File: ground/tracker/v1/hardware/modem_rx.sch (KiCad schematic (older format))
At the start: 15 parts, among them IC1 TCM3105, X1 4.4336 MHz

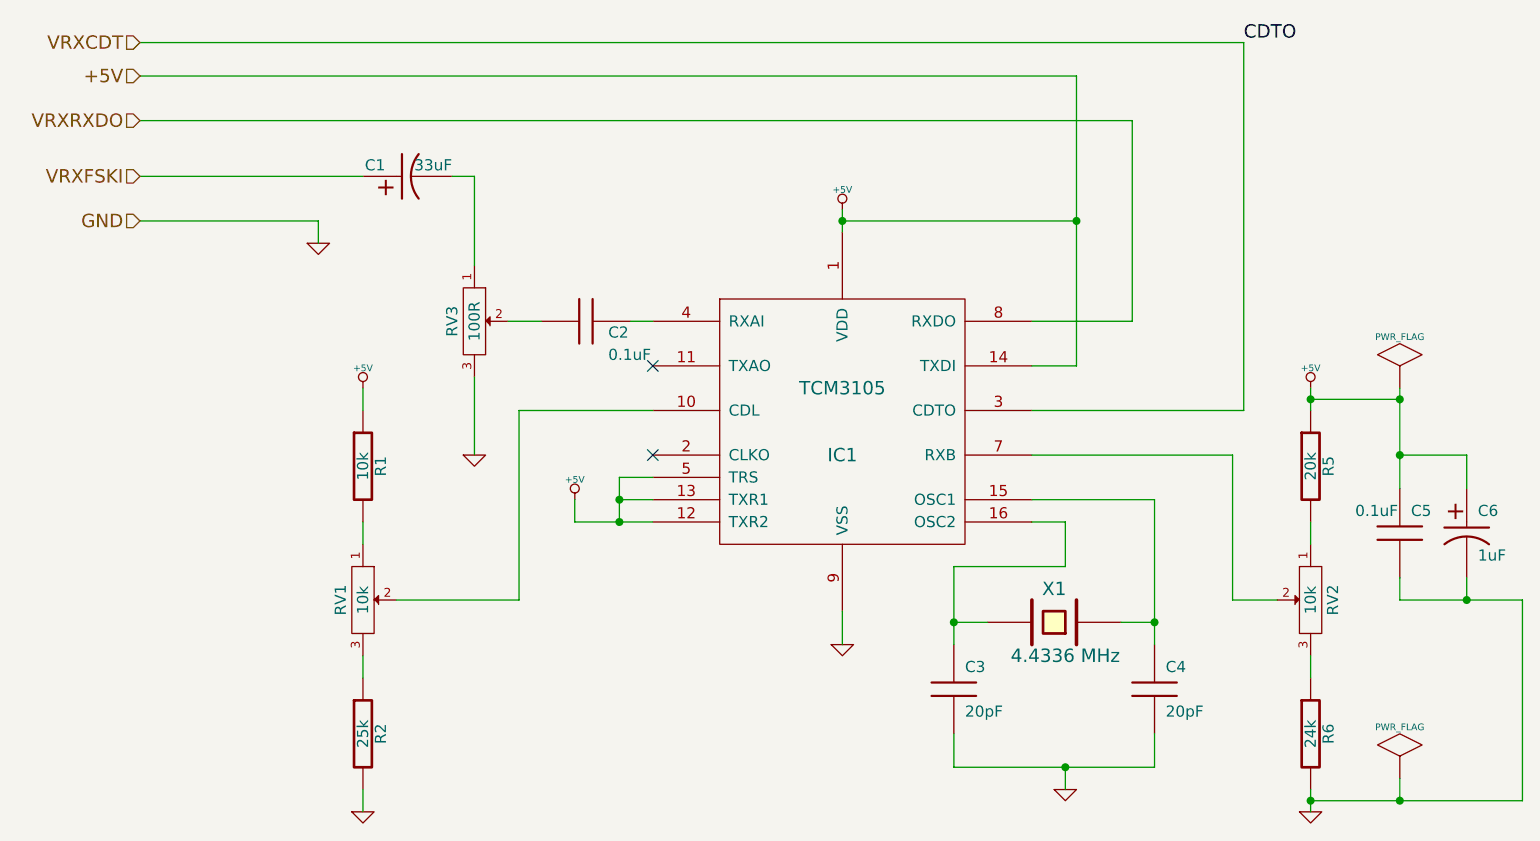
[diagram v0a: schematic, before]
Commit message: incorporated digital fsk demod routine, got flashhing lights, indicating getting data, now to test if tracking.EDIT: Tested in garden, and seems to track ok so fp context appears to be saving correctly^X
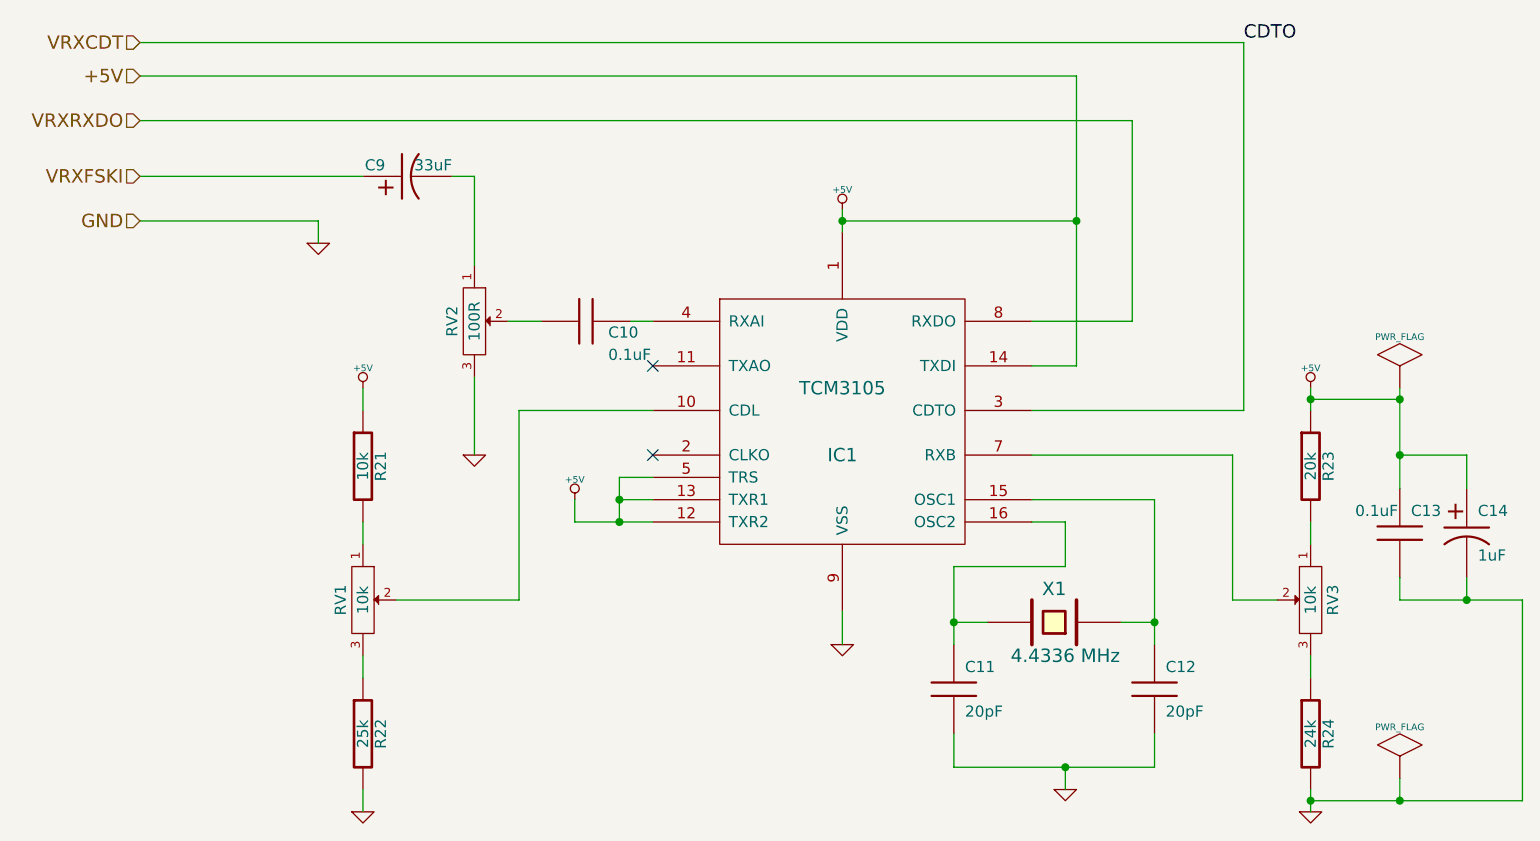
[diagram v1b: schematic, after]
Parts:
- renumbered C2 to C10, C3 to C11, C4 to C12, C5 to C13, C6 to C14, C1 to C9, R1 to R21, R2 to R22, R5 to R23, R6 to R24, RV3 to RV2, RV2 to RV3
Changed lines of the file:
@@
-EESchema Schematic File Version 2  date Thu 03 Jul 2014 10:08:41 BST
+EESchema Schematic File Version 2  date Sun 03 Aug 2014 18:59:40 BST
 LIBS:quantracker
 LIBS:stm32
@@
 Sheet 2 2
 Title ""
-Date "3 jul 2014"
+Date "3 aug 2014"
 Rev ""
 Comp ""
@@
 VRXFSKI
 $Comp
-L POT RV3
+L POT RV2
 U 1 1 53089937
 P 3850 3000
-F 0 "RV3" H 3850 2900 50  0000 C CNN
+F 0 "RV2" H 3850 2900 50  0000 C CNN
 F 1 "100R" H 3850 3000 50  0000 C CNN
 	1    3850 3000
@@
 $EndComp
 $Comp
-L CP1 C6
+L CP1 C14
 U 1 1 5305FE8F
 P 8300 3950
-F 0 "C6" H 8350 4050 50  0000 L CNN
+F 0 "C14" H 8350 4050 50  0000 L CNN
 F 1 "1uF" H 8350 3850 50  0000 L CNN
 	1    8300 3950
@@
 $EndComp
 $Comp
-L C C5
+L C C13
 U 1 1 5305FDEF
 P 8000 3950
-F 0 "C5" H 8050 4050 50  0000 L CNN
+F 0 "C13" H 8050 4050 50  0000 L CNN
 F 1 "0.1uF" H 7800 4050 50  0000 L CNN
 	1    8000 3950
@@
 $EndComp
 $Comp
-L CP1 C1
+L CP1 C9
 U 1 1 5305BDD5
 P 3550 2350
-F 0 "C1" V 3600 2450 50  0000 L CNN
+F 0 "C9" V 3600 2450 50  0000 L CNN
 F 1 "33uF" V 3600 2150 50  0000 L CNN
 	1    3550 2350
@@
 $EndComp
 $Comp
-L PWR_FLAG #FLG01
+L PWR_FLAG #FLG2
 U 1 1 5305AF9A
 P 8000 5050
-F 0 "#FLG01" H 8000 5320 30  0001 C CNN
+F 0 "#FLG2" H 8000 5320 30  0001 C CNN
 F 1 "PWR_FLAG" H 8000 5280 30  0000 C CNN
 	1    8000 5050
@@
 $EndComp
 $Comp
-L PWR_FLAG #FLG02
+L PWR_FLAG #FLG1
 U 1 1 5305AF8F
 P 8000 3300
-F 0 "#FLG02" H 8000 3570 30  0001 C CNN
+F 0 "#FLG1" H 8000 3570 30  0001 C CNN
 F 1 "PWR_FLAG" H 8000 3530 30  0000 C CNN
 	1    8000 3300
@@
 $EndComp
 $Comp
-L GND #PWR04
+L GND #PWR19
 U 1 1 526EA773
 P 3150 2650
-F 0 "#PWR04" H 3150 2650 30  0001 C CNN
+F 0 "#PWR19" H 3150 2650 30  0001 C CNN
 F 1 "GND" H 3150 2580 30  0001 C CNN
 	1    3150 2650
@@
 NoConn ~ 4650 3200
 $Comp
-L +5V #PWR05
+L +5V #PWR24
 U 1 1 526EA4DE
 P 5500 2500
-F 0 "#PWR05" H 5500 2590 20  0001 C CNN
+F 0 "#PWR24" H 5500 2590 20  0001 C CNN
 F 1 "+5V" H 5500 2590 30  0000 C CNN
 	1    5500 2500
@@
 $EndComp
 $Comp
-L +5V #PWR06
+L +5V #PWR27
 U 1 1 526EA4DB
 P 7600 3300
-F 0 "#PWR06" H 7600 3390 20  0001 C CNN
+F 0 "#PWR27" H 7600 3390 20  0001 C CNN
 F 1 "+5V" H 7600 3390 30  0000 C CNN
 	1    7600 3300
@@
 $EndComp
 $Comp
-L GND #PWR07
+L GND #PWR28
 U 1 1 526EA4D7
 P 7600 5200
-F 0 "#PWR07" H 7600 5200 30  0001 C CNN
+F 0 "#PWR28" H 7600 5200 30  0001 C CNN
 F 1 "GND" H 7600 5130 30  0001 C CNN
 	1    7600 5200
@@
 $EndComp
 $Comp
-L GND #PWR08
+L GND #PWR21
 U 1 1 526EA4D1
 P 3350 5200
-F 0 "#PWR08" H 3350 5200 30  0001 C CNN
+F 0 "#PWR21" H 3350 5200 30  0001 C CNN
 F 1 "GND" H 3350 5130 30  0001 C CNN
 	1    3350 5200
@@
 $EndComp
 $Comp
-L +5V #PWR09
+L +5V #PWR20
 U 1 1 526EA4CE
 P 3350 3300
-F 0 "#PWR09" H 3350 3390 20  0001 C CNN
+F 0 "#PWR20" H 3350 3390 20  0001 C CNN
 F 1 "+5V" H 3350 3390 30  0000 C CNN
 	1    3350 3300
@@
 $EndComp
 $Comp
-L GND #PWR010
+L GND #PWR22
 U 1 1 526EA493
 P 3850 3600
-F 0 "#PWR010" H 3850 3600 30  0001 C CNN
+F 0 "#PWR22" H 3850 3600 30  0001 C CNN
 F 1 "GND" H 3850 3530 30  0001 C CNN
 	1    3850 3600
@@
 $EndComp
 $Comp
-L GND #PWR011
+L GND #PWR25
 U 1 1 526EA430
 P 5500 4450
-F 0 "#PWR011" H 5500 4450 30  0001 C CNN
+F 0 "#PWR25" H 5500 4450 30  0001 C CNN
 F 1 "GND" H 5500 4380 30  0001 C CNN
 	1    5500 4450
@@
 $EndComp
 $Comp
-L GND #PWR012
+L GND #PWR26
 U 1 1 526EA414
 P 6500 5100
-F 0 "#PWR012" H 6500 5100 30  0001 C CNN
+F 0 "#PWR26" H 6500 5100 30  0001 C CNN
 F 1 "GND" H 6500 5030 30  0001 C CNN
 	1    6500 5100
@@
 $EndComp
 $Comp
-L +5V #PWR013
+L +5V #PWR23
 U 1 1 526EA35B
 P 4300 3800
-F 0 "#PWR013" H 4300 3890 20  0001 C CNN
+F 0 "#PWR23" H 4300 3890 20  0001 C CNN
 F 1 "+5V" H 4300 3890 30  0000 C CNN
 	1    4300 3800
@@
 $EndComp
 $Comp
-L R R6
+L R R24
 U 1 1 526E9F06
 P 7600 4850
-F 0 "R6" V 7680 4850 50  0000 C CNN
+F 0 "R24" V 7680 4850 50  0000 C CNN
 F 1 "24k" V 7600 4850 50  0000 C CNN
 	1    7600 4850
@@
 $EndComp
 $Comp
-L R R2
+L R R22
 U 1 1 526E9F03
 P 3350 4850
-F 0 "R2" V 3430 4850 50  0000 C CNN
+F 0 "R22" V 3430 4850 50  0000 C CNN
 F 1 "25k" V 3350 4850 50  0000 C CNN
 	1    3350 4850
@@
 $EndComp
 $Comp
-L R R5
+L R R23
 U 1 1 526E9EE9
 P 7600 3650
-F 0 "R5" V 7680 3650 50  0000 C CNN
+F 0 "R23" V 7680 3650 50  0000 C CNN
 F 1 "20k" V 7600 3650 50  0000 C CNN
 	1    7600 3650
@@
 $EndComp
 $Comp
-L R R1
+L R R21
 U 1 1 526E9EE5
 P 3350 3650
-F 0 "R1" V 3430 3650 50  0000 C CNN
+F 0 "R21" V 3430 3650 50  0000 C CNN
 F 1 "10k" V 3350 3650 50  0000 C CNN
 	1    3350 3650
@@
 $EndComp
 $Comp
-L POT RV2
+L POT RV3
 U 1 1 526E9E09
 P 7600 4250
-F 0 "RV2" H 7600 4150 50  0000 C CNN
+F 0 "RV3" H 7600 4150 50  0000 C CNN
 F 1 "10k" H 7600 4250 50  0000 C CNN
 	1    7600 4250
@@
 $EndComp
 $Comp
-L C C4
+L C C12
 U 1 1 526E9CC9
 P 6900 4650
-F 0 "C4" H 6950 4750 50  0000 L CNN
+F 0 "C12" H 6950 4750 50  0000 L CNN
 F 1 "20pF" H 6950 4550 50  0000 L CNN
 	1    6900 4650
@@
 $EndComp
 $Comp
-L C C3
+L C C11
 U 1 1 526E9CC3
 P 6000 4650
-F 0 "C3" H 6050 4750 50  0000 L CNN
+F 0 "C11" H 6050 4750 50  0000 L CNN
 F 1 "20pF" H 6050 4550 50  0000 L CNN
 	1    6000 4650
@@
 $EndComp
 $Comp
-L C C2
+L C C10
 U 1 1 526E9C9A
 P 4350 3000
-F 0 "C2" V 4400 3100 50  0000 L CNN
+F 0 "C10" V 4400 3100 50  0000 L CNN
 F 1 "0.1uF" V 4500 3100 50  0000 L CNN
 	1    4350 3000
